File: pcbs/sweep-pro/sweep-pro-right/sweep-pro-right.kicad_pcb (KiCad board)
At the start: 2 copper layers, 115 x 86.7 mm, 50 parts, among them J1 Conn_01x04_Female, J2 Conn_01x04_Female, J3 expantion1, SW1 SW_PUSH-kbd, SW10 SW_PUSH-kbd, SW11 SW_PUSH-kbd, SW12 SW_PUSH-kbd, SW13 SW_PUSH-kbd, SW14 SW_PUSH-kbd, SW15 SW_PUSH-kbd, SW16 SW_PUSH-kbd, SW17 SW_PUSH-kbd, SW2 SW_PUSH-kbd, SW3 SW_PUSH-kbd, SW4 SW_PUSH-kbd, SW5 SW_PUSH-kbd, SW6 SW_PUSH-kbd, SW7 SW_PUSH-kbd, SW8 SW_PUSH-kbd, SW9 SW_PUSH-kbd, U1 ProMicro-kbd

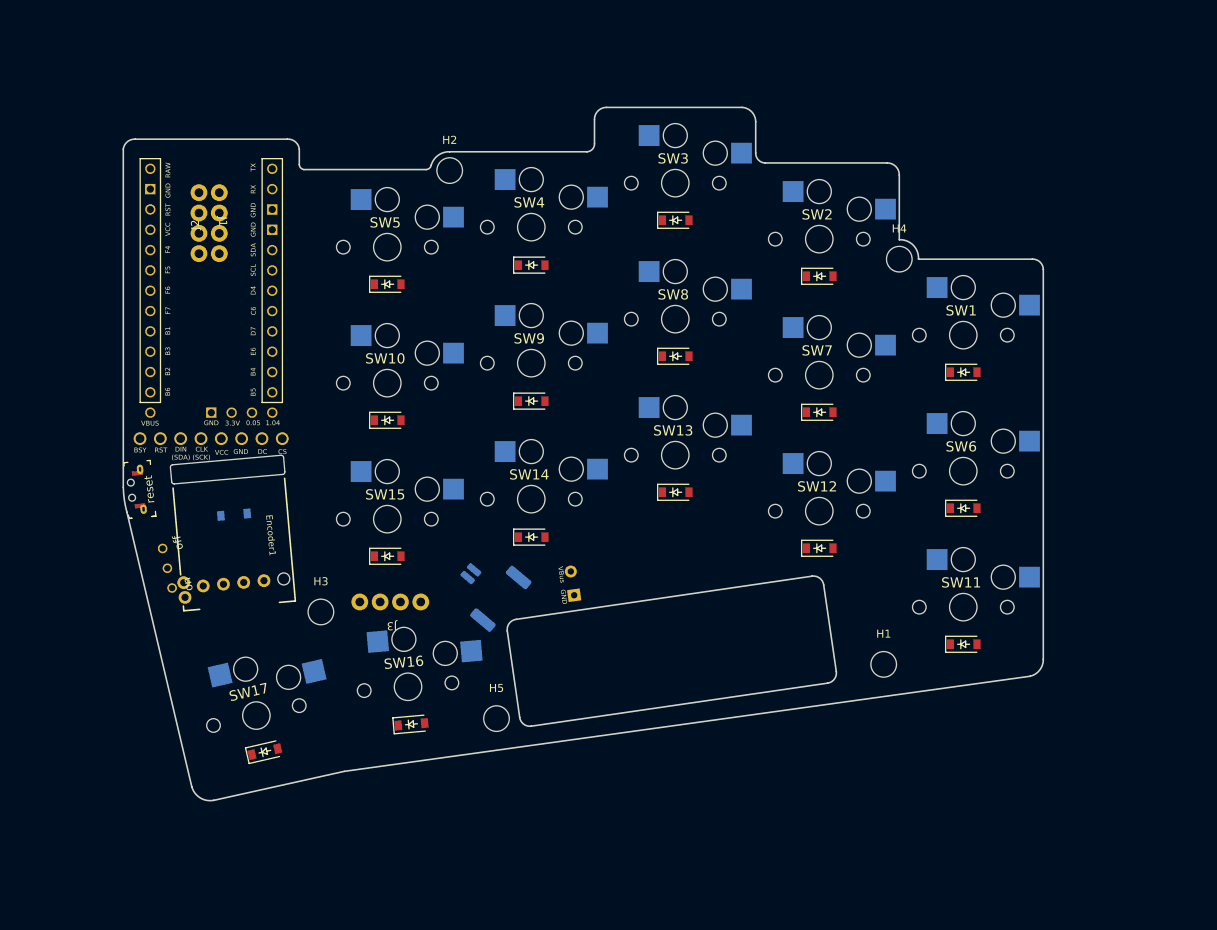
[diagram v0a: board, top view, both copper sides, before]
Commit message: sweepro v2
1. add three expansion ports (pogopin connection)
2. remev battery extra port
3. use nrfmacro-lite partial footprint
4. new power switch
5. re-position reset button
6. seperate board for left and right split
7. more symmetric layout of the encoders
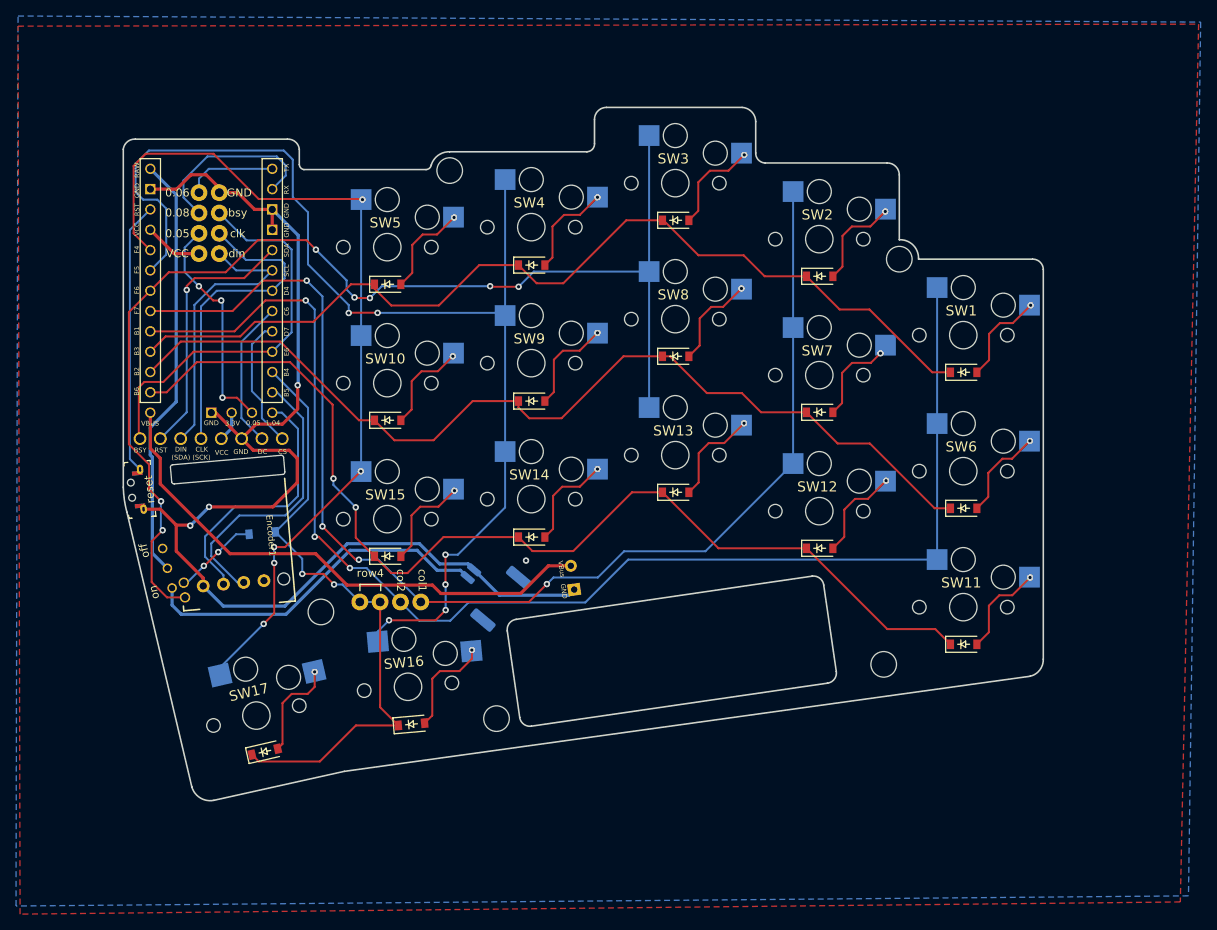
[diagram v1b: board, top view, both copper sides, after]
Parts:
- moved D18 4.21 mm to (100.1, 94.1), turned to -175 degrees
- moved WirelessCharger1 0.71 mm to (138.9, 99.7)
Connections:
- Display1 pad vcc: VCC -> 3.3V
- U1 pad 21: unconnected-(U1-Pad21) -> VCC
- U1 pad 29: VCC -> 3.3V
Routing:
- net col1: track 0.00 -> 170.3 mm, vias 0 -> 3
- net GND: track 0.00 -> 156.7 mm, vias 0 -> 4
- net col2: track 0.00 -> 156.6 mm, vias 0 -> 4
- net col3: track 0.00 -> 148.9 mm, vias 0 -> 7
- net col4: track 0.00 -> 148.0 mm, vias 0 -> 6
- net row3: track 0.00 -> 134.0 mm, vias 0 -> 2
- net row2: track 0.00 -> 121.2 mm
- net row1: track 0.00 -> 119.1 mm
- net col5: track 0.00 -> 110.8 mm, vias 0 -> 5
- net row4: track 0.00 -> 78.2 mm, vias 0 -> 2
- net VBus: track 0.00 -> 67.8 mm
- net VRaw: track 0.00 -> 53.5 mm
- net bsy: track 0.00 -> 49.7 mm
- net VBat: track 0.00 -> 44.3 mm
- net clk: track 0.00 -> 40.0 mm
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- added copper zone on B.Cu, net GND
- added copper zone on F.Cu, net GND
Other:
- outline, holes or cut-outs redrawn
